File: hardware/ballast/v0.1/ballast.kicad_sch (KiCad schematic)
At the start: 24 parts, among them J1 DALI, Q1 NX138BKR, U1 ICE40UP5K-SG48ITR, U2 SPI-Flash_EP, U3 140357145300, U4 140357145300

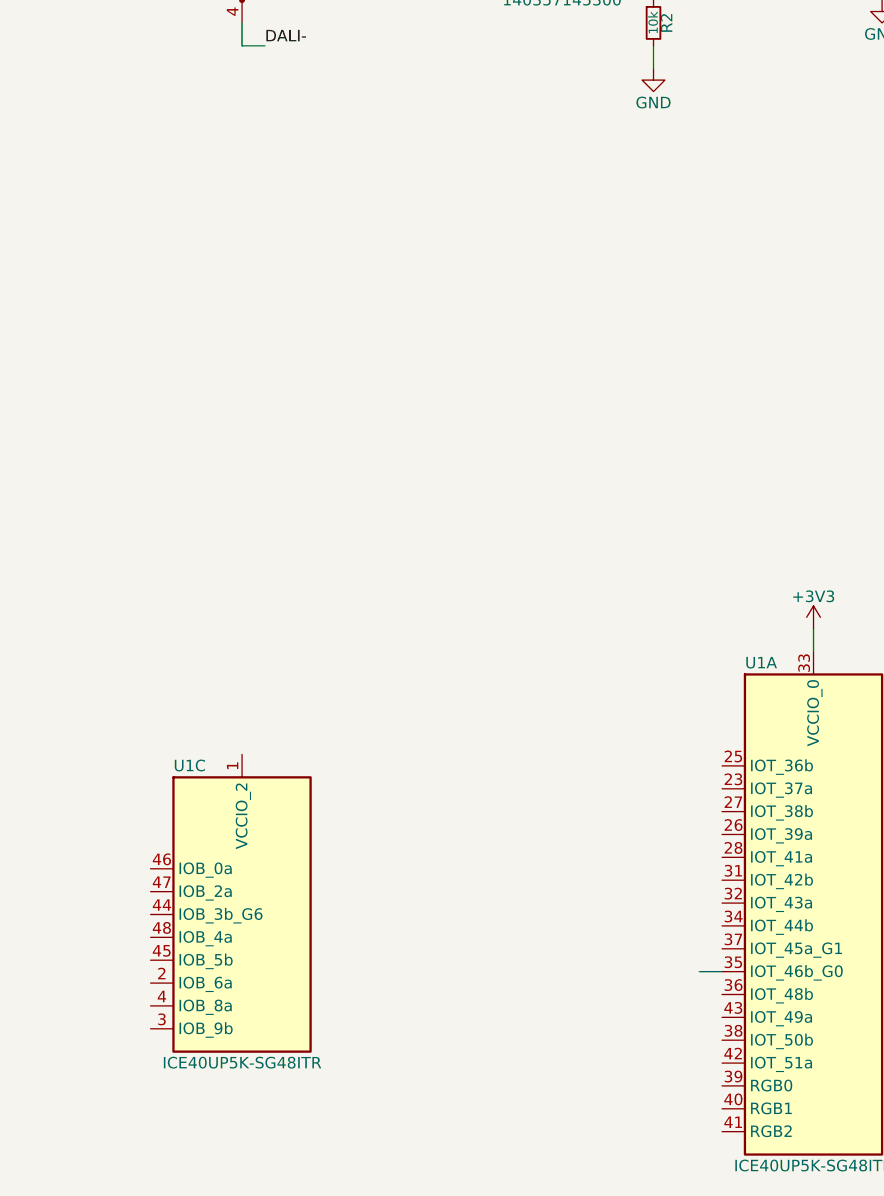
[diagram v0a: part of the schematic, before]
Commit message: Added the FRAM for persisting DALI config to the board
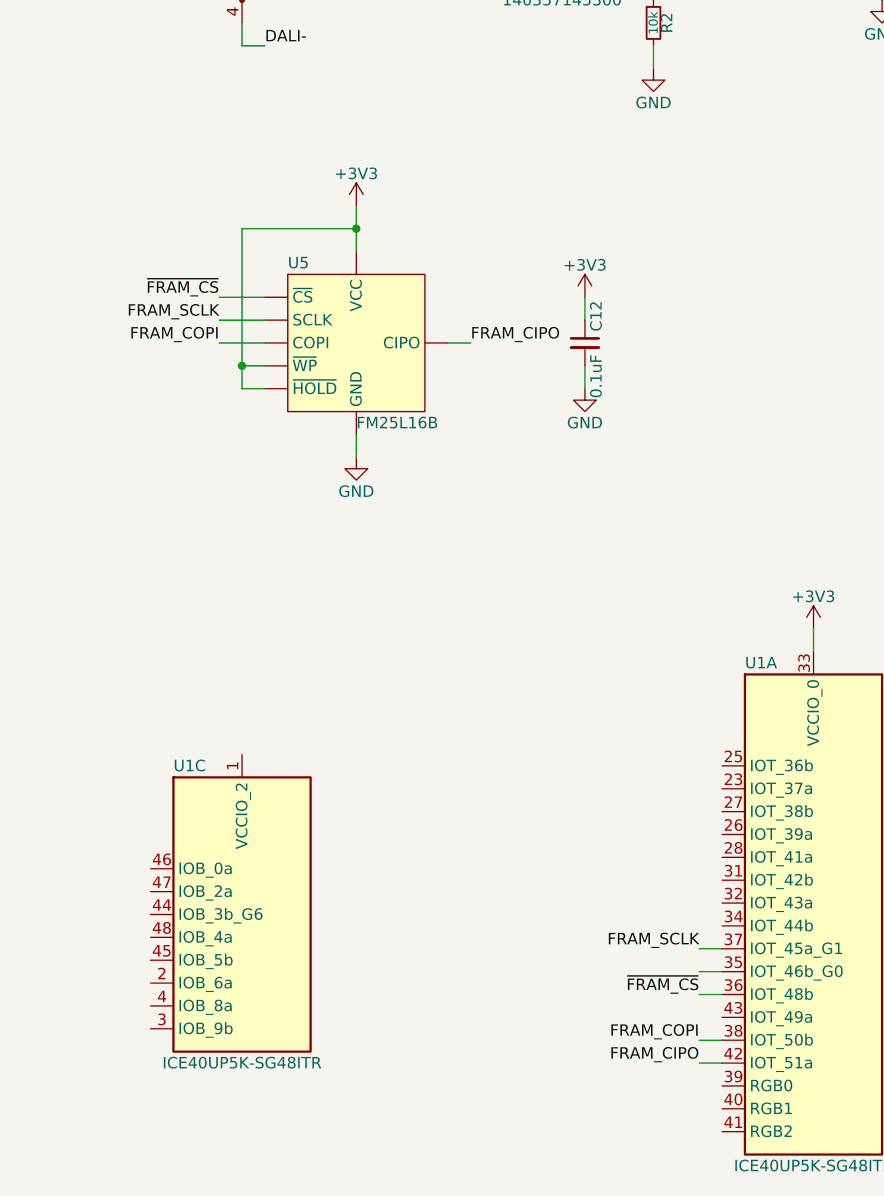
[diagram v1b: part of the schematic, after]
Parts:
- added C12: 0.1uF, rhais_rcl:C0603, symbol Device:C_Small
- added U5: FM25L16B, rhais_package-qfn:WDFN-8-1EP_4x4.5mm_P0.95mm_EP2.6x3.6mm, symbol DX-MON:FM25L16B
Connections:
- net +3V3: now also C12.1, U5.3 (~{WP}), U5.7 (~{HOLD}), U5.8 (VCC)
- net GND: now also C12.2, U5.4 (GND)
- net ~{FRAM_CS}: now reaches U1.36 (IOT_48b)
- net ~{FRAM_CS}: now also U5.1 (~{CS})
- net FRAM_SCLK: now reaches U1.37 (IOT_45a_G1)
- net FRAM_SCLK: now also U5.6 (SCLK)
- net FRAM_COPI: now reaches U1.38 (IOT_50b)
- net FRAM_COPI: now also U5.5 (COPI)
- net FRAM_CIPO: now reaches U1.42 (IOT_51a)
- net FRAM_CIPO: now also U5.2 (CIPO)
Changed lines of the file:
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@@
 (kicad_sch (version 20210621) (generator eeschema)
   (paper "A4")
+  (junction (at 63.5 91.44) (diameter 0) (color 0 0 0 0))
+  (junction (at 76.2 76.2) (diameter 0) (color 0 0 0 0))
   (junction (at 109.22 48.26) (diameter 0) (color 0 0 0 0))
   (junction (at 154.94 48.26) (diameter 0) (color 0 0 0 0))
@@
     (stroke (width 0) (type solid) (color 0 0 0 0))
   )
+  (wire (pts (xy 63.5 76.2) (xy 63.5 91.44))
+    (stroke (width 0) (type default) (color 0 0 0 0))
+  )
+  (wire (pts (xy 63.5 91.44) (xy 66.04 91.44))
+    (stroke (width 0) (type default) (color 0 0 0 0))
+  )
+  (wire (pts (xy 63.5 93.98) (xy 63.5 91.44))
+    (stroke (width 0) (type default) (color 0 0 0 0))
+  )
+  (wire (pts (xy 66.04 83.82) (xy 60.96 83.82))
+    (stroke (width 0) (type default) (color 0 0 0 0))
+  )
+  (wire (pts (xy 66.04 86.36) (xy 60.96 86.36))
+    (stroke (width 0) (type default) (color 0 0 0 0))
+  )
+  (wire (pts (xy 66.04 88.9) (xy 60.96 88.9))
+    (stroke (width 0) (type default) (color 0 0 0 0))
+  )
+  (wire (pts (xy 66.04 93.98) (xy 63.5 93.98))
+    (stroke (width 0) (type default) (color 0 0 0 0))
+  )
   (wire (pts (xy 71.12 45.72) (xy 73.66 45.72))
     (stroke (width 0) (type solid) (color 0 0 0 0))
@@
     (stroke (width 0) (type solid) (color 0 0 0 0))
   )
+  (wire (pts (xy 76.2 73.66) (xy 76.2 76.2))
+    (stroke (width 0) (type default) (color 0 0 0 0))
+  )
+  (wire (pts (xy 76.2 76.2) (xy 63.5 76.2))
+    (stroke (width 0) (type default) (color 0 0 0 0))
+  )
+  (wire (pts (xy 76.2 78.74) (xy 76.2 76.2))
+    (stroke (width 0) (type default) (color 0 0 0 0))
+  )
+  (wire (pts (xy 76.2 99.06) (xy 76.2 101.6))
+    (stroke (width 0) (type default) (color 0 0 0 0))
+  )
   (wire (pts (xy 86.36 33.02) (xy 88.9 33.02))
     (stroke (width 0) (type solid) (color 0 0 0 0))
@@
     (stroke (width 0) (type solid) (color 0 0 0 0))
   )
+  (wire (pts (xy 86.36 88.9) (xy 88.9 88.9))
+    (stroke (width 0) (type default) (color 0 0 0 0))
+  )
   (wire (pts (xy 88.9 35.56) (xy 88.9 33.02))
     (stroke (width 0) (type solid) (color 0 0 0 0))
@@
     (stroke (width 0) (type solid) (color 0 0 0 0))
   )
+  (wire (pts (xy 101.6 83.82) (xy 101.6 86.36))
+    (stroke (width 0) (type default) (color 0 0 0 0))
+  )
+  (wire (pts (xy 101.6 91.44) (xy 101.6 93.98))
+    (stroke (width 0) (type default) (color 0 0 0 0))
+  )
   (wire (pts (xy 106.68 43.18) (xy 109.22 43.18))
     (stroke (width 0) (type solid) (color 0 0 0 0))
@@
     (stroke (width 0) (type solid) (color 0 0 0 0))
   )
+  (wire (pts (xy 114.3 156.21) (xy 116.84 156.21))
+    (stroke (width 0) (type default) (color 0 0 0 0))
+  )
   (wire (pts (xy 114.3 158.75) (xy 116.84 158.75))
     (stroke (width 0) (type solid) (color 0 0 0 0))
+  )
+  (wire (pts (xy 114.3 161.29) (xy 116.84 161.29))
+    (stroke (width 0) (type default) (color 0 0 0 0))
+  )
+  (wire (pts (xy 114.3 166.37) (xy 116.84 166.37))
+    (stroke (width 0) (type default) (color 0 0 0 0))
+  )
+  (wire (pts (xy 114.3 168.91) (xy 116.84 168.91))
+    (stroke (width 0) (type default) (color 0 0 0 0))
   )
   (wire (pts (xy 127 120.65) (xy 127 123.19))
@@
     (effects (font (size 1.27 1.27)) (justify left bottom))
   )
+  (label "~{FRAM_CS}" (at 60.96 83.82 180)
+    (effects (font (size 1.27 1.27)) (justify right bottom))
+  )
+  (label "FRAM_SCLK" (at 60.96 86.36 180)
+    (effects (font (size 1.27 1.27)) (justify right bottom))
+  )
+  (label "FRAM_COPI" (at 60.96 88.9 180)
+    (effects (font (size 1.27 1.27)) (justify right bottom))
+  )
   (label "DALI+" (at 66.04 33.02 0)
     (effects (font (size 1.27 1.27)) (justify left bottom))
@@
     (effects (font (size 1.27 1.27)) (justify right bottom))
   )
+  (label "FRAM_CIPO" (at 88.9 88.9 0)
+    (effects (font (size 1.27 1.27)) (justify left bottom))
+  )
   (label "DALI_RX" (at 111.76 48.26 0)
     (effects (font (size 1.27 1.27)) (justify left bottom))
   )
+  (label "FRAM_SCLK" (at 114.3 156.21 180)
+    (effects (font (size 1.27 1.27)) (justify right bottom))
+  )
+  (label "~{FRAM_CS}" (at 114.3 161.29 180)
+    (effects (font (size 1.27 1.27)) (justify right bottom))
+  )
+  (label "FRAM_COPI" (at 114.3 166.37 180)
+    (effects (font (size 1.27 1.27)) (justify right bottom))
+  )
+  (label "FRAM_CIPO" (at 114.3 168.91 180)
+    (effects (font (size 1.27 1.27)) (justify right bottom))
+  )
   (label "DALI_TX" (at 127 43.18 180)
     (effects (font (size 1.27 1.27)) (justify right bottom))
@@
     (effects (font (size 1.27 1.27)) (justify right bottom))
   )
+  (symbol (lib_id "power:+3V3") (at 76.2 73.66 0) (unit 1)
+    (in_bom yes) (on_board yes)
+    (property "Reference" "#PWR08" (id 0) (at 76.2 77.47 0)
+      (effects (font (size 1.27 1.27)) hide)
+    )
+    (property "Value" "+3V3" (id 1) (at 76.2 70.104 0))
+    (property "Footprint" "" (id 2) (at 76.2 73.66 0)
+      (effects (font (size 1.27 1.27)) hide)
+    )
+    (property "Datasheet" "" (id 3) (at 76.2 73.66 0)
+      (effects (font (size 1.27 1.27)) hide)
+    )
+    (pin "1")
+  )
+  (symbol (lib_id "power:+3V3") (at 101.6 83.82 0) (unit 1)
+    (in_bom yes) (on_board yes)
+    (property "Reference" "#PWR015" (id 0) (at 101.6 87.63 0)
+      (effects (font (size 1.27 1.27)) hide)
+    )
+    (property "Value" "+3V3" (id 1) (at 101.6 80.264 0))
+    (property "Footprint" "" (id 2) (at 101.6 83.82 0)
+      (effects (font (size 1.27 1.27)) hide)
+    )
+    (property "Datasheet" "" (id 3) (at 101.6 83.82 0)
+      (effects (font (size 1.27 1.27)) hide)
+    )
+    (pin "1")
+  )
   (symbol (lib_id "power:+3V3") (at 109.22 40.64 0) (unit 1)
     (in_bom yes) (on_board yes)
@@
     (pin "1")
   )
+  (symbol (lib_id "power:GND") (at 76.2 101.6 0) (unit 1)
+    (in_bom yes) (on_board yes)
+    (property "Reference" "#PWR014" (id 0) (at 76.2 107.95 0)
+      (effects (font (size 1.27 1.27)) hide)
+    )
+    (property "Value" "GND" (id 1) (at 76.2 105.41 0))
+    (property "Footprint" "" (id 2) (at 76.2 101.6 0)
+      (effects (font (size 1.27 1.27)) hide)
+    )
+    (property "Datasheet" "" (id 3) (at 76.2 101.6 0)
+      (effects (font (size 1.27 1.27)) hide)
+    )
+    (pin "1")
+  )
+  (symbol (lib_id "power:GND") (at 101.6 93.98 0) (unit 1)
+    (in_bom yes) (on_board yes)
+    (property "Reference" "#PWR016" (id 0) (at 101.6 100.33 0)
+      (effects (font (size 1.27 1.27)) hide)
+    )
+    (property "Value" "GND" (id 1) (at 101.6 97.79 0))
+    (property "Footprint" "" (id 2) (at 101.6 93.98 0)
+      (effects (font (size 1.27 1.27)) hide)
+    )
+    (property "Datasheet" "" (id 3) (at 101.6 93.98 0)
+      (effects (font (size 1.27 1.27)) hide)
+    )
+    (pin "1")
+  )
   (symbol (lib_id "power:GND") (at 109.22 58.42 0) (unit 1)
     (in_bom yes) (on_board yes)
@@
     )
     (property "Datasheet" "~" (id 3) (at 256.54 109.22 0)
+      (effects (font (size 1.27 1.27)) hide)
+    )
+    (pin "1")
+    (pin "2")
+  )
+  (symbol (lib_id "Device:C_Small") (at 101.6 88.9 0) (unit 1)
+    (in_bom yes) (on_board yes)
+    (property "Reference" "C12" (id 0) (at 102.87 87.63 90)
+      (effects (font (size 1.27 1.27)) (justify left))
+    )
+    (property "Value" "0.1uF" (id 1) (at 102.87 90.17 90)
+      (effects (font (size 1.27 1.27)) (justify right))
+    )
+    (property "Footprint" "rhais_rcl:C0603" (id 2) (at 101.6 88.9 0)
+      (effects (font (size 1.27 1.27)) hide)
+    )
+    (property "Datasheet" "~" (id 3) (at 101.6 88.9 0)
       (effects (font (size 1.27 1.27)) hide)
     )
@@
     (pin "8")
     (pin "9")
+  )
+  (symbol (lib_id "DX-MON:FM25L16B") (at 76.2 88.9 0) (unit 1)
+    (in_bom yes) (on_board yes)
+    (property "Reference" "U5" (id 0) (at 68.58 80.01 0)
+      (effects (font (size 1.27 1.27)) (justify left))
+    )
+    (property "Value" "FM25L16B" (id 1) (at 76.2 97.79 0)
+      (effects (font (size 1.27 1.27)) (justify left))
+    )
+    (property "Footprint" "rhais_package-qfn:WDFN-8-1EP_4x4.5mm_P0.95mm_EP2.6x3.6mm" (id 2) (at 76.2 88.9 0)
+      (effects (font (size 1.27 1.27)) hide)
+    )
+    (property "Datasheet" "" (id 3) (at 76.2 88.9 0)
+      (effects (font (size 1.27 1.27)) hide)
+    )
+    (pin "1")
+    (pin "2")
+    (pin "3")
+    (pin "4")
+    (pin "5")
+    (pin "6")
+    (pin "7")
+    (pin "8")
   )
   (symbol (lib_id "FPGA_Lattice:ICE40UP5K-SG48ITR") (at 63.5 152.4 0) (unit 3)
@@
       (reference "#PWR07") (unit 1) (value "GND") (footprint "")
     )
+    (path "/a912844a-9670-42fd-ab55-1c08b567e5fa"
+      (reference "#PWR08") (unit 1) (value "+3V3") (footprint "")
+    )
     (path "/ef13737e-ae48-4c69-911b-b05c5f599835"
       (reference "#PWR09") (unit 1) (value "+3V3") (footprint "")
@@
       (reference "#PWR013") (unit 1) (value "GND") (footprint "")
     )
+    (path "/2e3cf577-5ee5-43a7-ba14-5cd173ac3a6a"
+      (reference "#PWR014") (unit 1) (value "GND") (footprint "")
+    )
+    (path "/5757e08c-42df-4fa2-bea9-e15a2b9e84ca"
+      (reference "#PWR015") (unit 1) (value "+3V3") (footprint "")
+    )
+    (path "/46a06d17-ba3e-4e73-90bf-66fad1c67e59"
+      (reference "#PWR016") (unit 1) (value "GND") (footprint "")
+    )
     (path "/f0481c54-85e3-4ff8-9637-5942dcad05ab"
       (reference "#PWR0101") (unit 1) (value "GND") (footprint "")
@@
       (reference "C11") (unit 1) (value "10uF") (footprint "rhais_rcl:C0603")
     )
+    (path "/8928e31a-ea5e-45f9-b767-828b26771e13"
+      (reference "C12") (unit 1) (value "0.1uF") (footprint "rhais_rcl:C0603")
+    )
     (path "/45388831-b5da-430e-87dd-5be560a083e1"
       (reference "D1") (unit 1) (value "D_Bridge_+-AA") (footprint "rhais_diode:Bridge_Bridge_DBL")
@@
       (reference "U4") (unit 1) (value "140357145300") (footprint "rhais_package-smd:SO-4_4.4x3.6mm_P2.54mm")
     )
-  )
+    (path "/539b073f-2894-40f7-ad93-7ff106b5a30f"
+      (reference "U5") (unit 1) (value "FM25L16B") (footprint "rhais_package-qfn:WDFN-8-1EP_4x4.5mm_P0.95mm_EP2.6x3.6mm")
+    )
+  )
